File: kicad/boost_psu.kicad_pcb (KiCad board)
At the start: 2 copper layers, 50 x 30 mm, 21 parts, among them J1 +12V, J2 HT, Q1 MPS751, Q2 IRF740, U1 MC34063AP

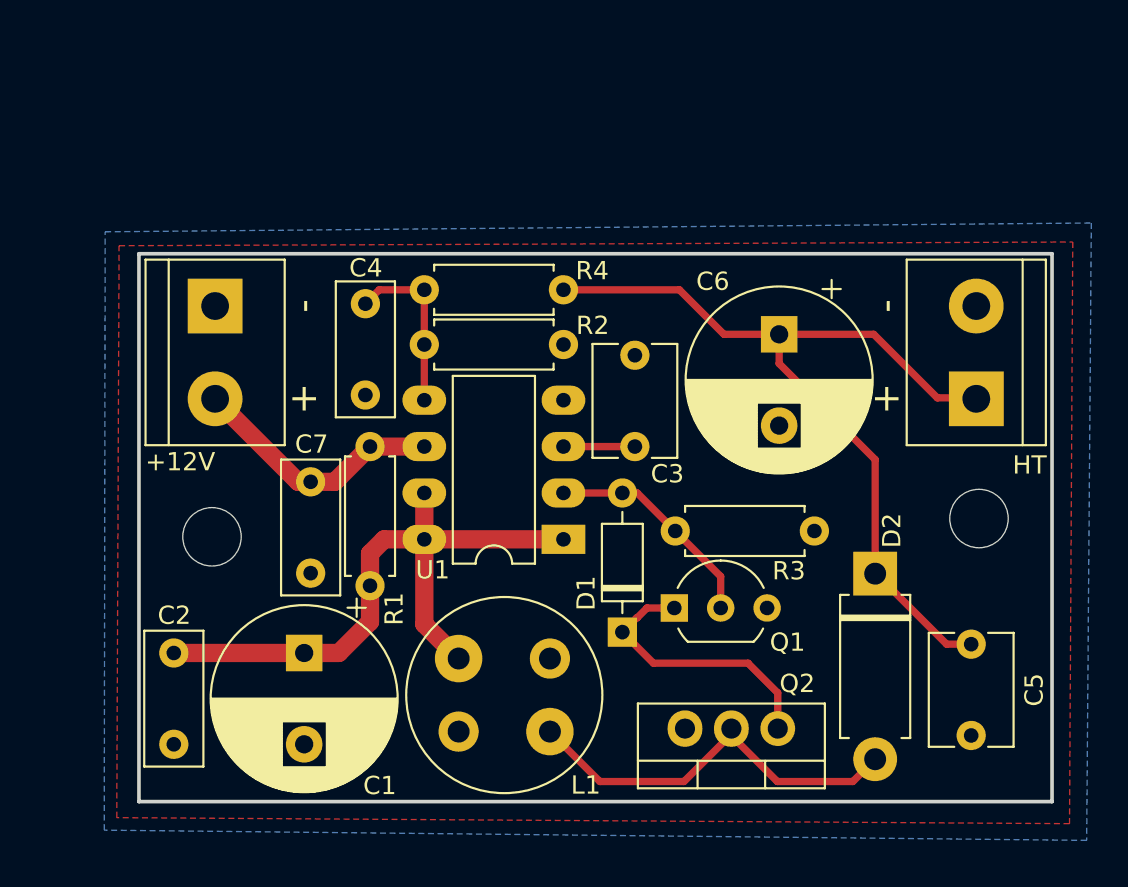
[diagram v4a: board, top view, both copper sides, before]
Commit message: Fix inductor footprint & improve layout
Signed-off-by: Arnaud Ferraris <arnaud.ferraris@gmail.com>
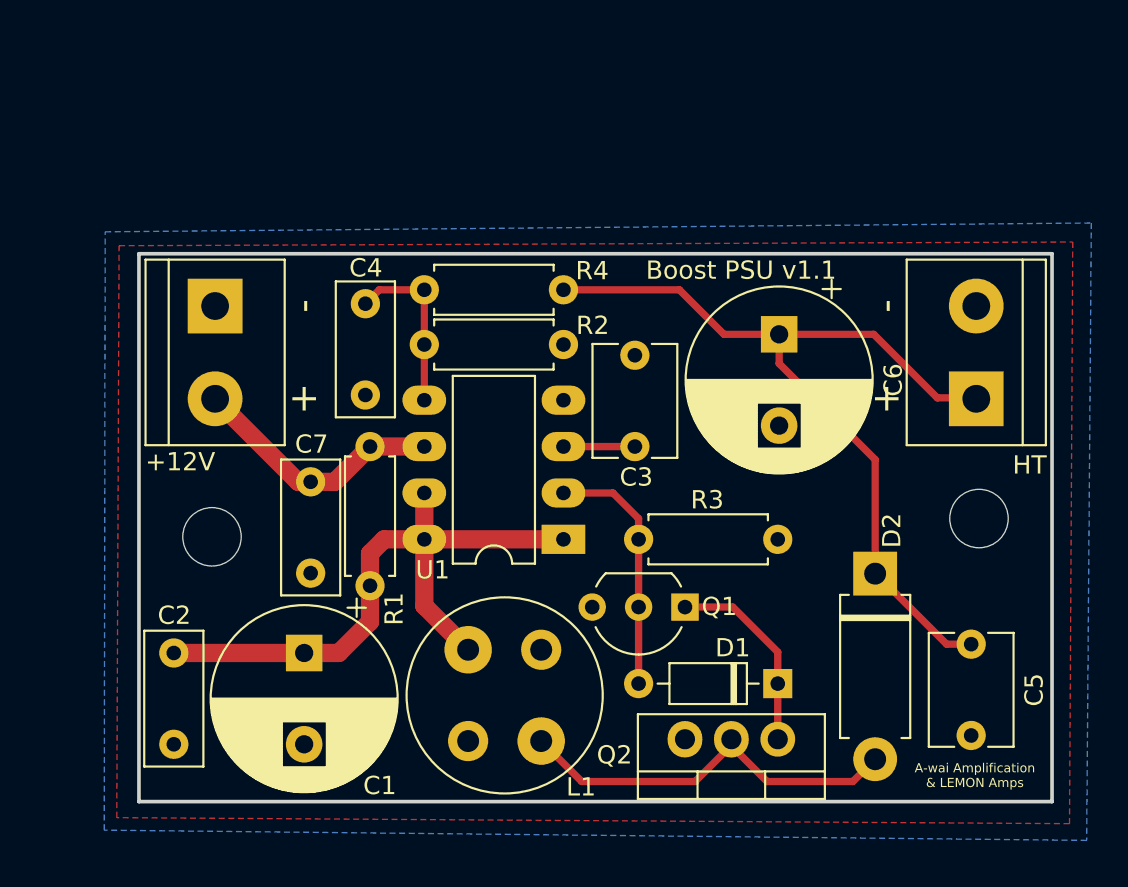
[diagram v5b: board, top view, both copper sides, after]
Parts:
- moved D1 8.96 mm to (175.0, 113.5), turned to 180 degrees
- moved R3 2.06 mm to (167.4, 105.6)
- moved L1 0.71 mm to (158.0, 111.7), turned to 0 degrees
- moved Q1 0.59 mm to (169.9, 109.3), turned to 180 degrees
- moved Q2 0.58 mm to (175.0, 116.6)
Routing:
- net Net-(D1-Pad1): track 15.2 -> 10.9 mm
- net Net-(D1-Pad2): track 12.2 -> 13.7 mm
- net /HT1: track 22.3 -> 21.7 mm
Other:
- board text added: "A-wai Amplification & LEMON Amps"
- board text added: "Boost PSU v1.1"
